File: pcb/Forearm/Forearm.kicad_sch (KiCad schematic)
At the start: 19 parts, among them J1 Conn_01x02, J2 Conn_01x16_Top, J3 Conn_01x16_Bottom, J9 Conn_01x01, U1 ESP32-S3-DEVKITC-1-N8R2, U2 4754

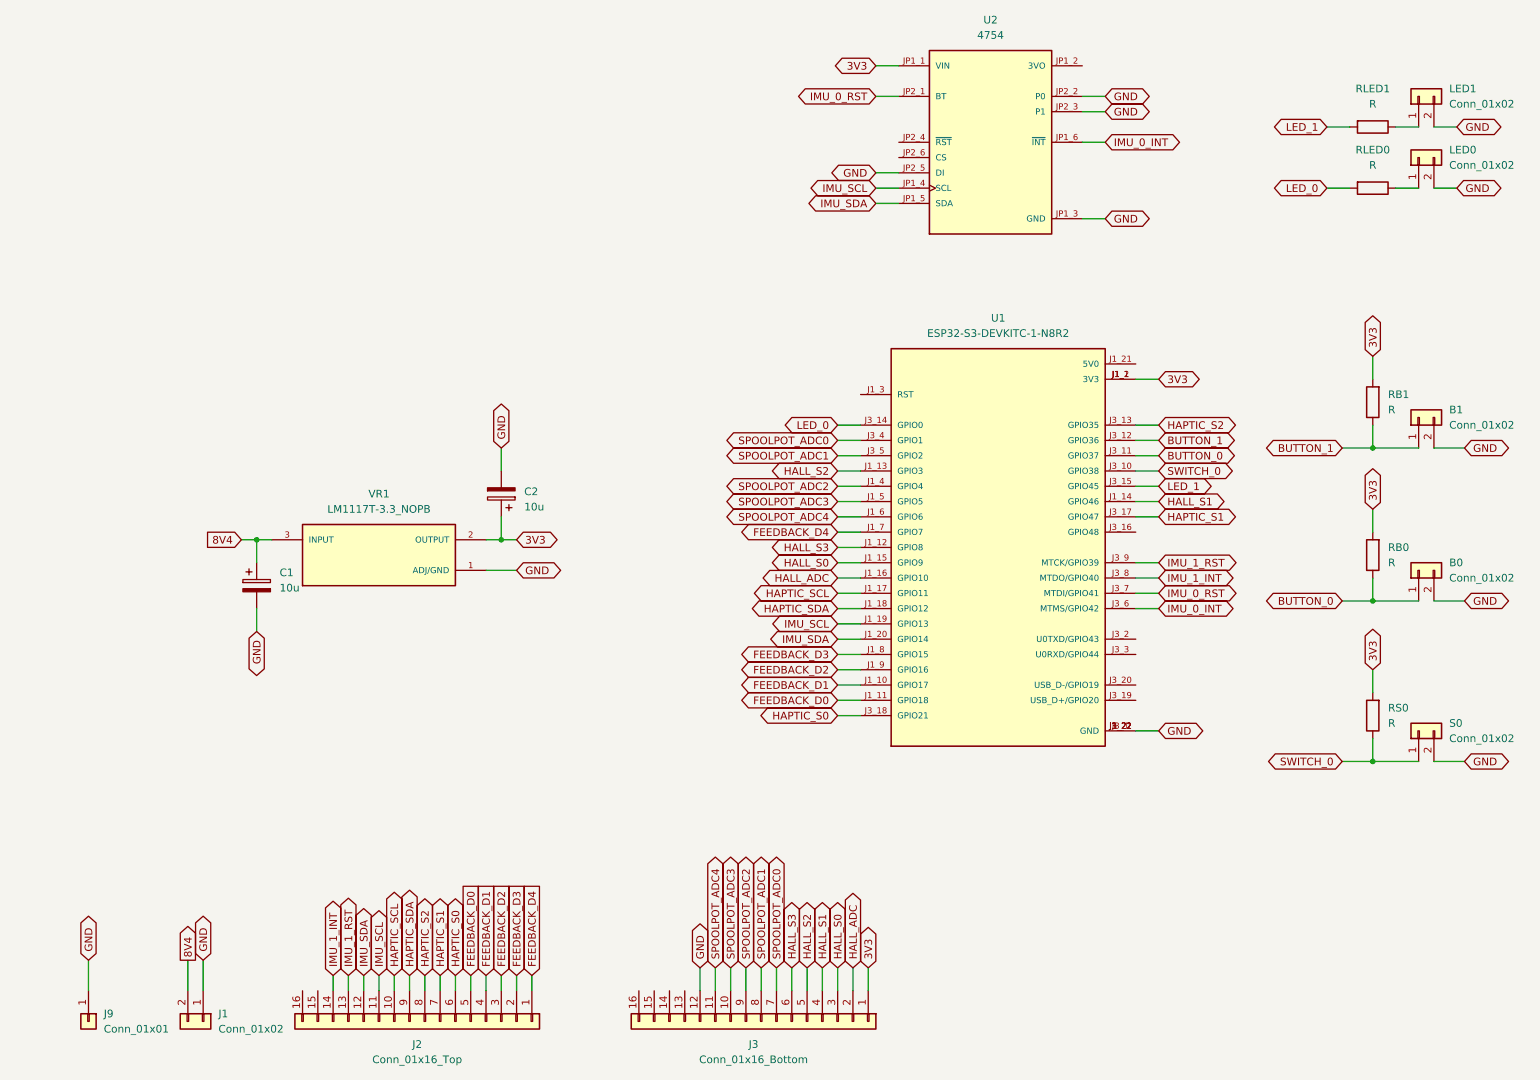
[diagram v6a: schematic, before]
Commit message: updated esp32 pins on schematic
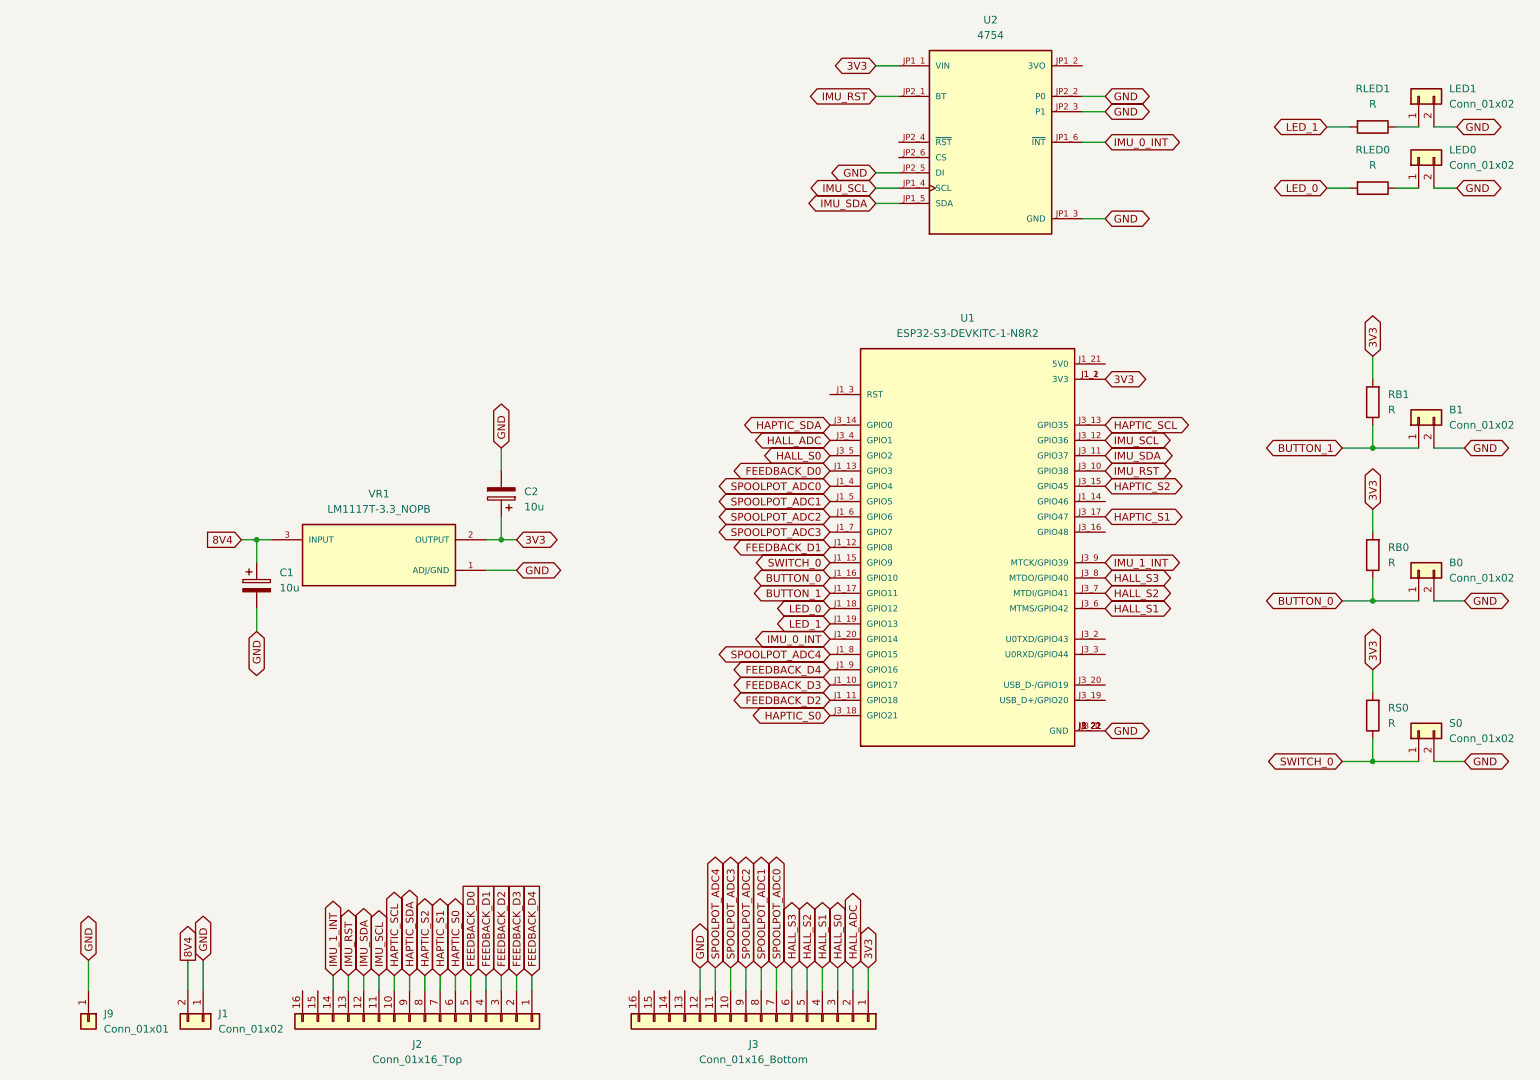
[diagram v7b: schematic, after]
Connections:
- net BUTTON_0: now also U1.J1_16 (GPIO10); no longer U1.J3_11 (GPIO37)
- net BUTTON_1: now also U1.J1_17 (GPIO11); no longer U1.J3_12 (GPIO36)
- net FEEDBACK_D0: now also U1.J1_13 (GPIO3); no longer U1.J1_11 (GPIO18)
- net FEEDBACK_D1: now also U1.J1_12 (GPIO8); no longer U1.J1_10 (GPIO17)
- net FEEDBACK_D2: now also U1.J1_11 (GPIO18); no longer U1.J1_9 (GPIO16)
- net FEEDBACK_D3: now also U1.J1_10 (GPIO17); no longer U1.J1_8 (GPIO15)
- net FEEDBACK_D4: now also U1.J1_9 (GPIO16); no longer U1.J1_7 (GPIO7)
- net HALL_ADC: now also U1.J3_4 (GPIO1); no longer U1.J1_16 (GPIO10)
- net HALL_S0: now also U1.J3_5 (GPIO2); no longer U1.J1_15 (GPIO9)
- net HALL_S1: now also U1.J3_6 (MTMS/GPIO42); no longer U1.J1_14 (GPIO46)
- net HALL_S2: now also U1.J3_7 (MTDI/GPIO41); no longer U1.J1_13 (GPIO3)
- net HALL_S3: now also U1.J3_8 (MTDO/GPIO40); no longer U1.J1_12 (GPIO8)
- net HAPTIC_S2: now also U1.J3_15 (GPIO45); no longer U1.J3_13 (GPIO35)
- net HAPTIC_SCL: now also U1.J3_13 (GPIO35); no longer U1.J1_17 (GPIO11)
- net HAPTIC_SDA: now also U1.J3_14 (GPIO0); no longer U1.J1_18 (GPIO12)
- net IMU_0_INT: now also U1.J1_20 (GPIO14); no longer U1.J3_6 (MTMS/GPIO42)
- net IMU_1_INT: now also U1.J3_9 (MTCK/GPIO39); no longer U1.J3_8 (MTDO/GPIO40)
- net IMU_SCL: now also U1.J3_12 (GPIO36); no longer U1.J1_19 (GPIO13)
- net IMU_SDA: now also U1.J3_11 (GPIO37); no longer U1.J1_20 (GPIO14)
- net LED_0: now also U1.J1_18 (GPIO12); no longer U1.J3_14 (GPIO0)
- net LED_1: now also U1.J1_19 (GPIO13); no longer U1.J3_15 (GPIO45)
- net SPOOLPOT_ADC0: now also U1.J1_4 (GPIO4); no longer U1.J3_4 (GPIO1)
- net SPOOLPOT_ADC1: now also U1.J1_5 (GPIO5); no longer U1.J3_5 (GPIO2)
- net SPOOLPOT_ADC2: now also U1.J1_6 (GPIO6); no longer U1.J1_4 (GPIO4)
- net SPOOLPOT_ADC3: now also U1.J1_7 (GPIO7); no longer U1.J1_5 (GPIO5)
- net SPOOLPOT_ADC4: now also U1.J1_8 (GPIO15); no longer U1.J1_6 (GPIO6)
- net SWITCH_0: now also U1.J1_15 (GPIO9); no longer U1.J3_10 (GPIO38)
- net IMU_0_RST renamed IMU_RST
- net IMU_RST: now also J2.13 (Pin_13), U1.J3_10 (GPIO38); no longer U1.J3_7 (MTDI/GPIO41)
- removed net IMU_1_RST: J2.13 (Pin_13), U1.J3_9 (MTCK/GPIO39)
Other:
- moved on the sheet: U1

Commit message: board done will upload to JCL to check for errors
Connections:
- net SPOOLPOT_ADC0: now also U1.J1_7 (GPIO7); no longer U1.J1_4 (GPIO4)
- net SPOOLPOT_ADC1: now also U1.J1_8 (GPIO15); no longer U1.J1_5 (GPIO5)
- net SPOOLPOT_ADC3: now also U1.J1_5 (GPIO5); no longer U1.J1_7 (GPIO7)
- net SPOOLPOT_ADC4: now also U1.J1_4 (GPIO4); no longer U1.J1_8 (GPIO15)
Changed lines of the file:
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@@
 		)
 	)
-	(global_label "SPOOLPOT_ADC4"
+	(global_label "SPOOLPOT_ADC1"
 		(shape bidirectional)
 		(at 162.56 128.27 180)
@@
 		)
 	)
-	(global_label "SPOOLPOT_ADC1"
+	(global_label "SPOOLPOT_ADC3"
 		(shape bidirectional)
 		(at 162.56 102.87 180)
@@
 		)
 	)
-	(global_label "SPOOLPOT_ADC3"
+	(global_label "SPOOLPOT_ADC0"
 		(shape bidirectional)
 		(at 162.56 107.95 180)
@@
 		)
 	)
-	(global_label "SPOOLPOT_ADC0"
+	(global_label "SPOOLPOT_ADC4"
 		(shape bidirectional)
 		(at 162.56 100.33 180)
